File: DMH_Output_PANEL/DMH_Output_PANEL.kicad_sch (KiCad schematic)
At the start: 16 parts, among them J0 Panel_GND_Solder_Wire_Pad

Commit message: Front panel design in progress
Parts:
- added H16: Clip L, SynthStuff:MountingHole_LED_3mm, symbol Mechanical:MountingHole
- added H17: Clip R, SynthStuff:MountingHole_LED_3mm, symbol Mechanical:MountingHole
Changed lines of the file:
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@@
+	)
+	(symbol
+		(lib_id "Mechanical:MountingHole")
+		(at 139.7 50.8 0)
+		(unit 1)
+		(exclude_from_sim no)
+		(in_bom no)
+		(on_board yes)
+		(dnp no)
+		(property "Reference" "H17"
+			(at 142.24 49.5299 0)
+			(effects
+				(font
+					(size 1.27 1.27)
+				)
+				(justify left)
+			)
+		)
+		(property "Value" "Clip R"
+			(at 142.24 52.0699 0)
+			(effects
+				(font
+					(size 1.27 1.27)
+					(thickness 0.254)
+					(bold yes)
+					(italic yes)
+				)
+				(justify left)
+			)
+		)
+		(property "Footprint" "SynthStuff:MountingHole_LED_3mm"
+			(at 139.7 50.8 0)
+			(effects
+				(font
+					(size 1.27 1.27)
+				)
+				(hide yes)
+			)
+		)
+		(property "Datasheet" "~"
+			(at 139.7 50.8 0)
+			(effects
+				(font
+					(size 1.27 1.27)
+				)
+				(hide yes)
+			)
+		)
+		(property "Description" "Mounting Hole LED 3mm"
+			(at 154.178 54.356 0)
+			(effects
+				(font
+					(size 1.27 1.27)
+				)
+			)
+		)
+		(instances
+			(project "DMH_Output_PANEL"
+				(path "/a552705f-a9fe-462e-9913-5cfcc08b233c"
+					(reference "H17")
+					(unit 1)
+				)
+			)
+		)
 	)
 	(symbol
@@
 					(unit 1)
 				)
+			)
+		)
+	)
+	(symbol
+		(lib_id "Mechanical:MountingHole")
+		(at 101.6 50.8 0)
+		(unit 1)
+		(exclude_from_sim no)
+		(in_bom no)
+		(on_board yes)
+		(dnp no)
+		(property "Reference" "H16"
+			(at 104.14 49.5299 0)
+			(effects
+				(font
+					(size 1.27 1.27)
+				)
+				(justify left)
+			)
+		)
+		(property "Value" "Clip L"
+			(at 104.14 52.0699 0)
+			(effects
+				(font
+					(size 1.27 1.27)
+					(thickness 0.254)
+					(bold yes)
+					(italic yes)
+				)
+				(justify left)
+			)
+		)
+		(property "Footprint" "SynthStuff:MountingHole_LED_3mm"
+			(at 101.6 50.8 0)
+			(effects
+				(font
+					(size 1.27 1.27)
+				)
+				(hide yes)
+			)
+		)
+		(property "Datasheet" "~"
+			(at 101.6 50.8 0)
+			(effects
+				(font
+					(size 1.27 1.27)
+				)
+				(hide yes)
+			)
+		)
+		(property "Description" "Mounting Hole LED 3mm"
+			(at 116.078 54.356 0)
+			(effects
+				(font
+					(size 1.27 1.27)
+				)
+			)
+		)
+		(instances
+			(project ""
+				(path "/a552705f-a9fe-462e-9913-5cfcc08b233c"
+					(reference "H16")
+					(unit 1)
+				)

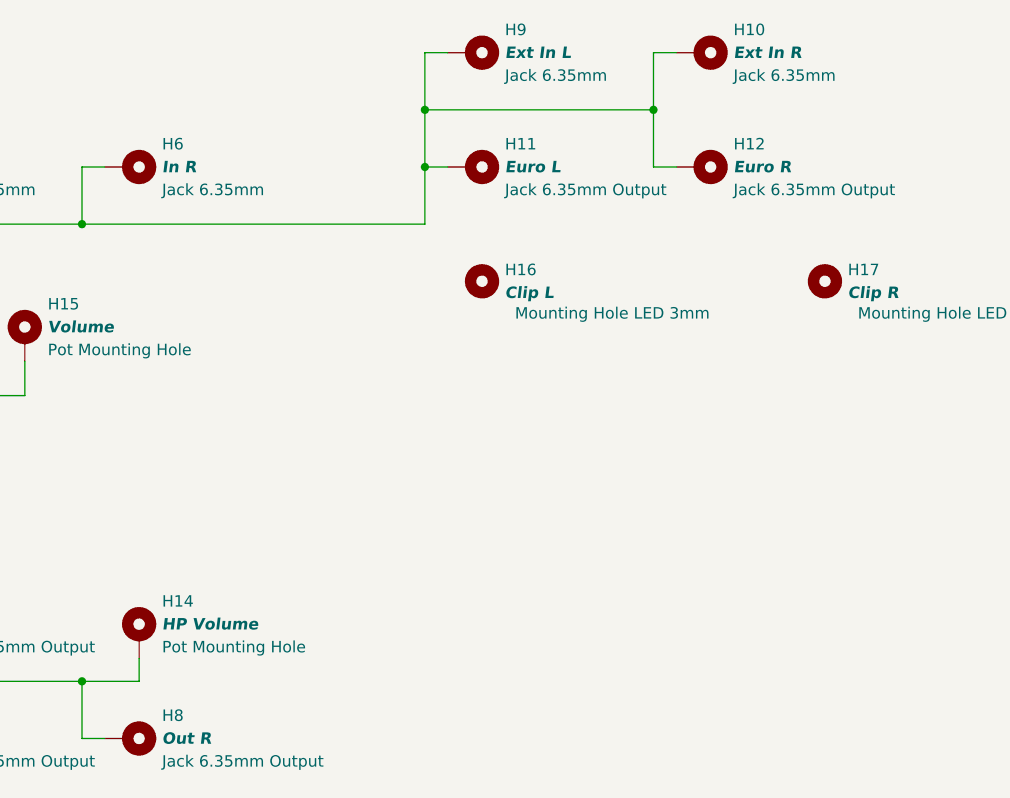
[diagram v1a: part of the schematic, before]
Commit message: Designed front panel
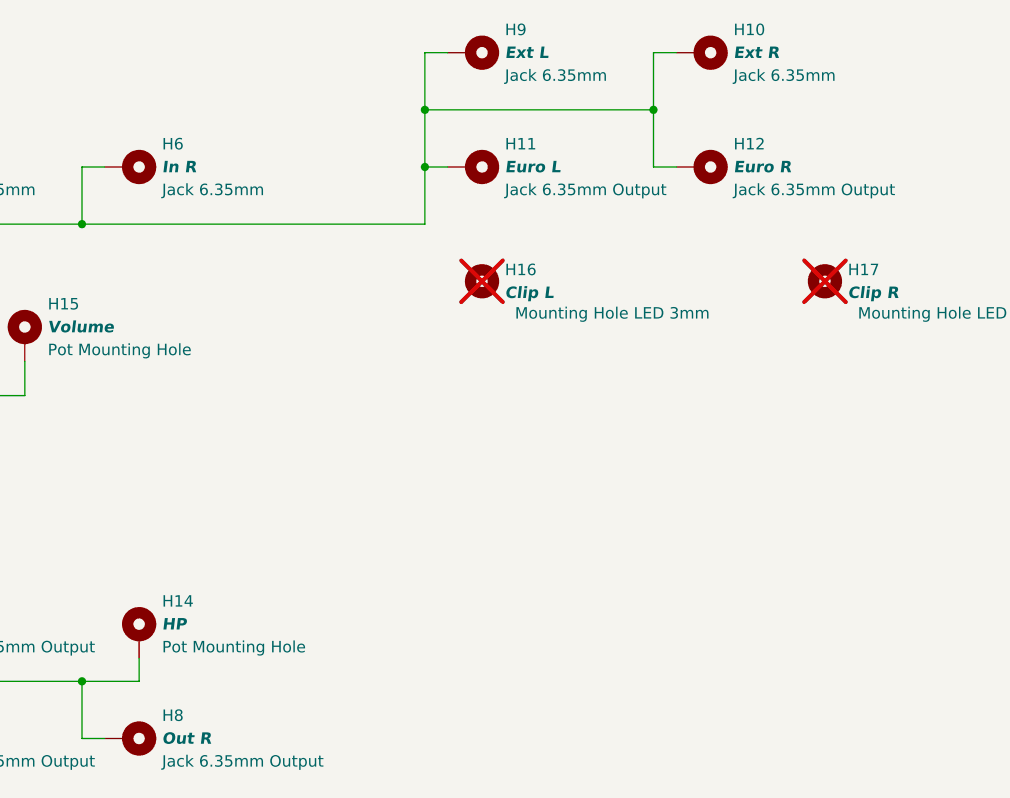
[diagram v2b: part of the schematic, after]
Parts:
- H10: value Ext In R -> Ext R
- H14: value HP Volume -> HP
- H16, H17: now not fitted
- H9: value Ext In L -> Ext L
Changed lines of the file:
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@@
 		(at 139.7 50.8 0)
 		(unit 1)
-		(exclude_from_sim no)
-		(in_bom no)
-		(on_board yes)
-		(dnp no)
+		(exclude_from_sim yes)
+		(in_bom no)
+		(on_board no)
+		(dnp yes)
 		(property "Reference" "H17"
 			(at 142.24 49.5299 0)
@@
 		(at 101.6 50.8 0)
 		(unit 1)
-		(exclude_from_sim no)
-		(in_bom no)
-		(on_board yes)
-		(dnp no)
+		(exclude_from_sim yes)
+		(in_bom no)
+		(on_board no)
+		(dnp yes)
 		(property "Reference" "H16"
 			(at 104.14 49.5299 0)
@@
 			)
 		)
-		(property "Value" "Ext In R"
+		(property "Value" "Ext R"
 			(at 129.54 25.4 0)
 			(effects
@@
 			)
 		)
-		(property "Value" "Ext In L"
+		(property "Value" "Ext L"
 			(at 104.14 25.4 0)
 			(effects
@@
 			)
 		)
-		(property "Value" "HP Volume"
+		(property "Value" "HP"
 			(at 66.04 88.9 0)
 			(effects

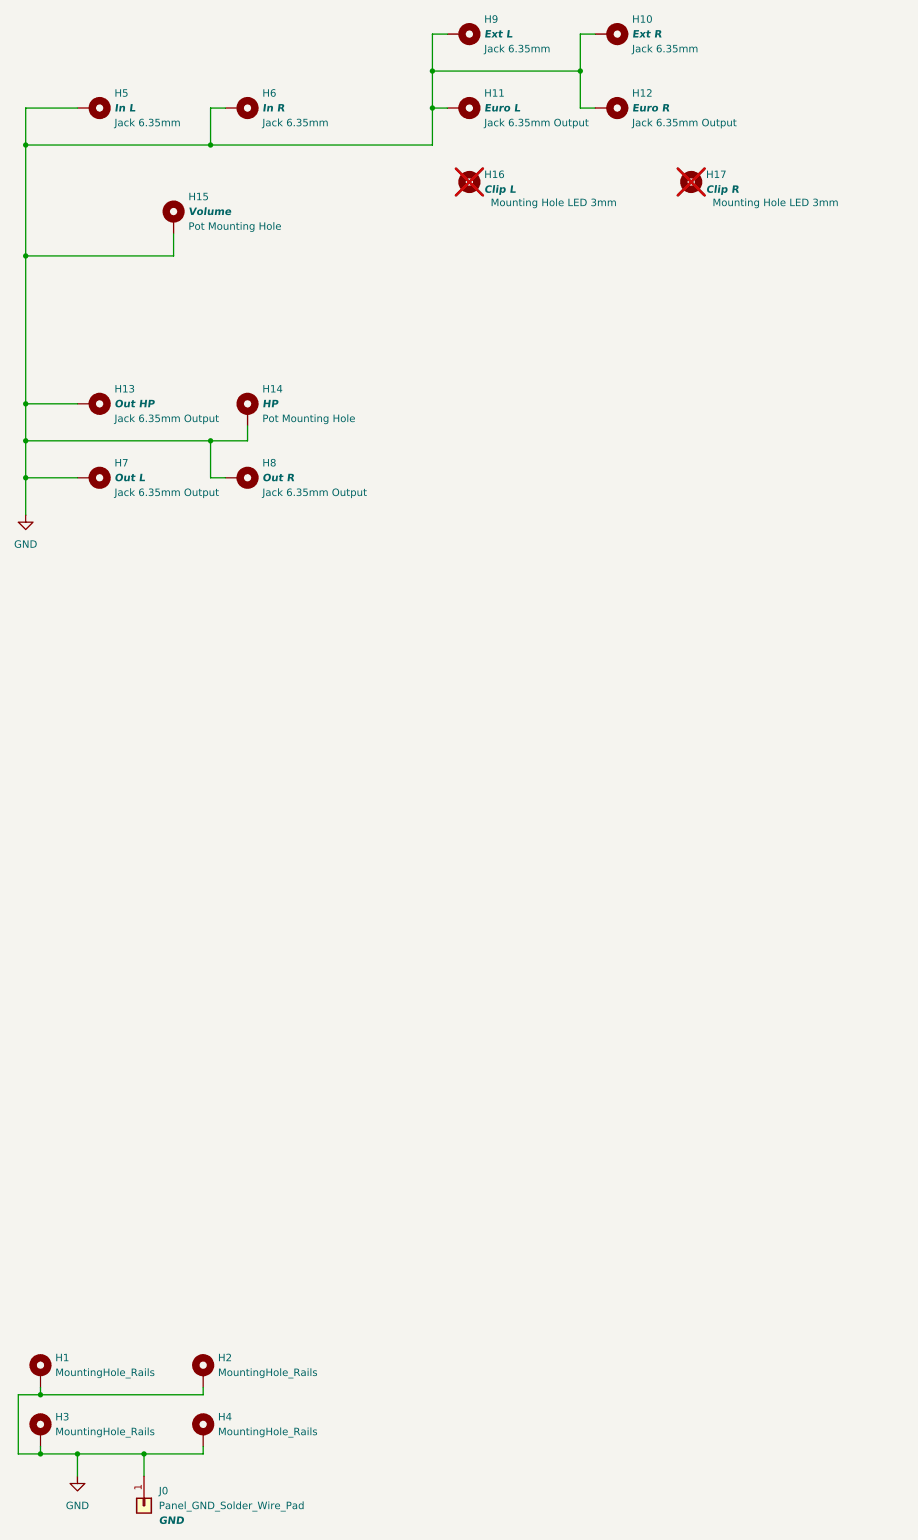
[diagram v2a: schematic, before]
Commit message: Finished front panel design
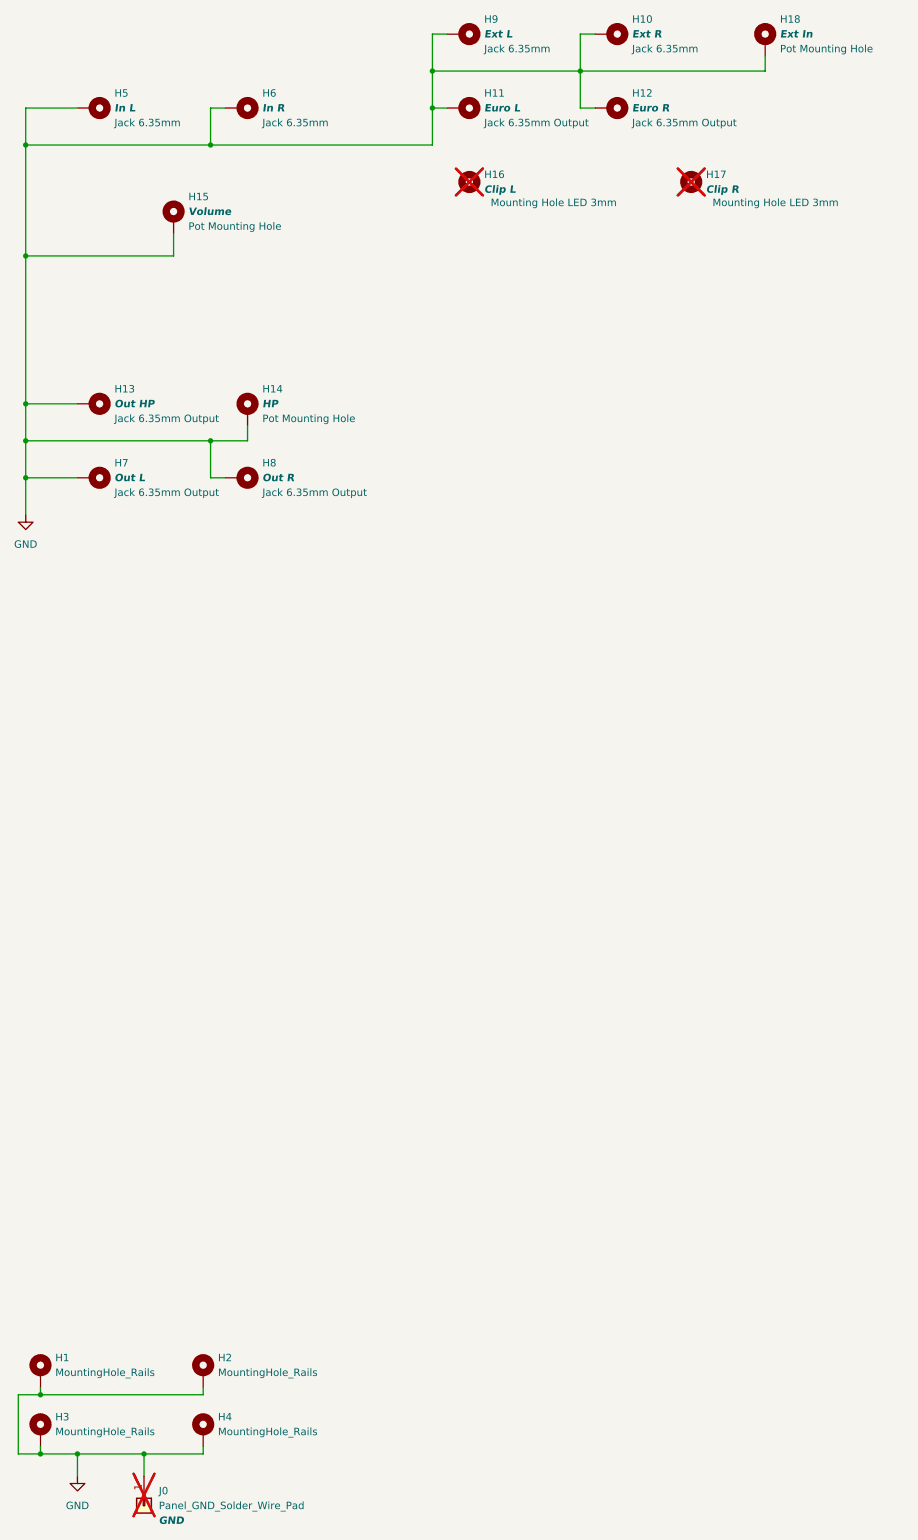
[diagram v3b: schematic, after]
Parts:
- added H18: Ext In, SynthStuff:Pot_Cutout_Tiny, symbol SynthStuff:MountingHole_Pot
- H15: footprint SynthStuff:Pot_Cutout_Medium -> SynthStuff:Pot_Cutout_Medium_v2
- J0: now not fitted
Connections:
- net GND: now also H18.1

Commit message: Centralized library
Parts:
- H16, H17: footprint SynthStuff:MountingHole_LED_3mm -> SynthStuff:MountingHole_LED_3mm_R
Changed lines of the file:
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@@
 		(at 139.7 50.8 0)
 		(unit 1)
-		(exclude_from_sim yes)
+		(exclude_from_sim no)
 		(in_bom no)
 		(on_board no)
@@
 			)
 		)
-		(property "Footprint" "SynthStuff:MountingHole_LED_3mm"
+		(property "Footprint" "SynthStuff:MountingHole_LED_3mm_R"
 			(at 139.7 50.8 0)
 			(effects
@@
 		(at 50.8 57.15 0)
 		(unit 1)
-		(exclude_from_sim yes)
+		(exclude_from_sim no)
 		(in_bom yes)
 		(on_board yes)
@@
 		(at 127 38.1 0)
 		(unit 1)
-		(exclude_from_sim yes)
+		(exclude_from_sim no)
 		(in_bom no)
 		(on_board yes)
@@
 		(at 38.1 38.1 0)
 		(unit 1)
-		(exclude_from_sim yes)
+		(exclude_from_sim no)
 		(in_bom no)
 		(on_board yes)
@@
 		(at 101.6 38.1 0)
 		(unit 1)
-		(exclude_from_sim yes)
+		(exclude_from_sim no)
 		(in_bom no)
 		(on_board yes)
@@
 		(at 101.6 50.8 0)
 		(unit 1)
-		(exclude_from_sim yes)
+		(exclude_from_sim no)
 		(in_bom no)
 		(on_board no)
@@
 			)
 		)
-		(property "Footprint" "SynthStuff:MountingHole_LED_3mm"
+		(property "Footprint" "SynthStuff:MountingHole_LED_3mm_R"
 			(at 101.6 50.8 0)
 			(effects
@@
 		(at 152.4 26.67 0)
 		(unit 1)
-		(exclude_from_sim yes)
+		(exclude_from_sim no)
 		(in_bom yes)
 		(on_board yes)
@@
 		(at 63.5 38.1 0)
 		(unit 1)
-		(exclude_from_sim yes)
+		(exclude_from_sim no)
 		(in_bom no)
 		(on_board yes)
@@
 		(at 127 25.4 0)
 		(unit 1)
-		(exclude_from_sim yes)
+		(exclude_from_sim no)
 		(in_bom no)
 		(on_board yes)
@@
 		(at 101.6 25.4 0)
 		(unit 1)
-		(exclude_from_sim yes)
+		(exclude_from_sim no)
 		(in_bom no)
 		(on_board yes)
@@
 		(at 38.1 101.6 0)
 		(unit 1)
-		(exclude_from_sim yes)
+		(exclude_from_sim no)
 		(in_bom no)
 		(on_board yes)
@@
 		(at 63.5 90.17 0)
 		(unit 1)
-		(exclude_from_sim yes)
+		(exclude_from_sim no)
 		(in_bom yes)
 		(on_board yes)
@@
 		(at 63.5 101.6 0)
 		(unit 1)
-		(exclude_from_sim yes)
+		(exclude_from_sim no)
 		(in_bom no)
 		(on_board yes)
@@
 		(at 45.72 278.13 270)
 		(unit 1)
-		(exclude_from_sim yes)
-		(in_bom no)
-		(on_board no)
+		(exclude_from_sim no)
+		(in_bom no)
+		(on_board yes)
 		(dnp yes)
 		(fields_autoplaced yes)
@@
 		(at 38.1 88.9 0)
 		(unit 1)
-		(exclude_from_sim yes)
-		(in_bom no)
-		(on_board yes)
+		(exclude_from_sim no)
+		(in_bom no)
+		(on_board yes)

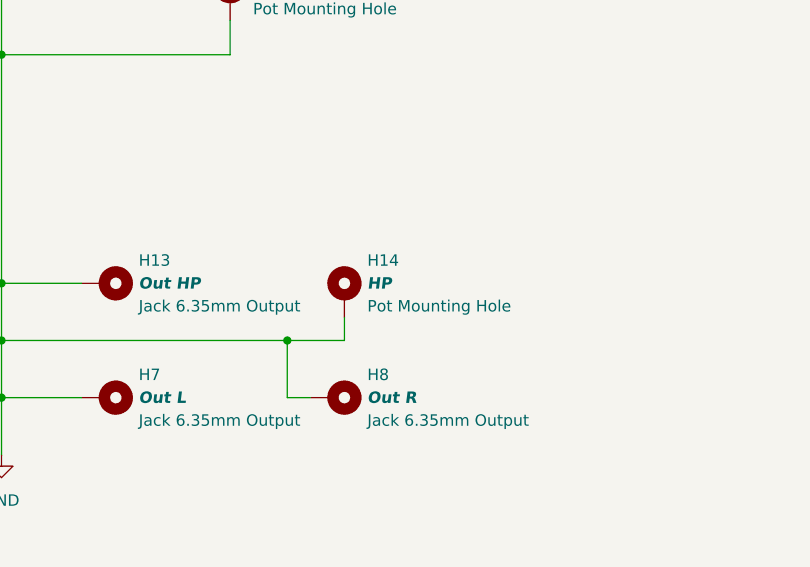
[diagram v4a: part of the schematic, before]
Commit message: Generated Gerbers for prototyping
Panel, Controls and LEDs only
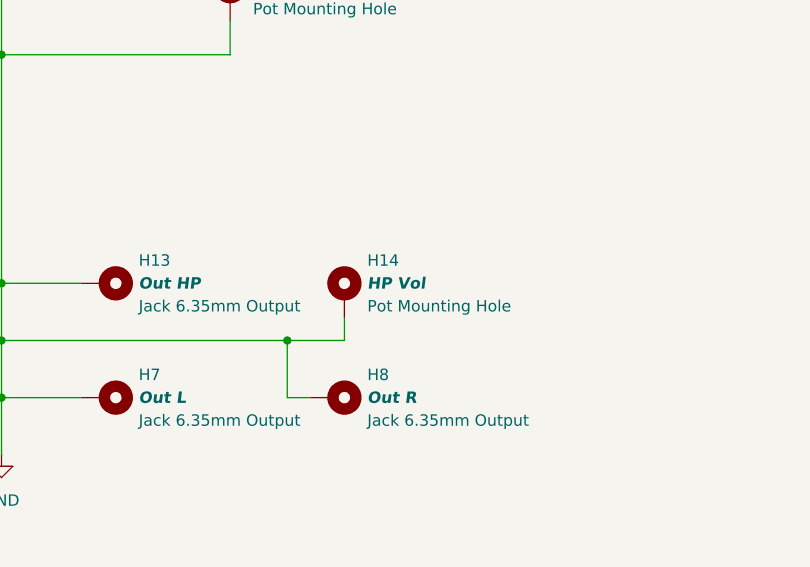
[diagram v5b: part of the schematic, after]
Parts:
- H14: value HP -> HP Vol
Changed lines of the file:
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@@
 			)
 		)
-		(property "Value" "HP"
+		(property "Value" "HP Vol"
 			(at 66.04 88.9 0)
 			(effects
